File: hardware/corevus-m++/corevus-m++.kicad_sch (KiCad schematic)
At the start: 156 parts, among them J1 USB 2.0, J4 Power In, J4 XH, J5 Power In, J5 XH, J6 1x2P, SW3 BOOT, SW3 RST, T1 3.3V, T1 CS, T1 Diag, T1 Dir, T1 En, T1 Gnd, T1 MISO, T1 MOSI, T1 SClk, T1 Step, T1 Therm, T1 V_{SA}, U1 AMS1117-3.3, U2 TPS61040DBV, U3 STM32H750VBTx, Y1 12 MHz

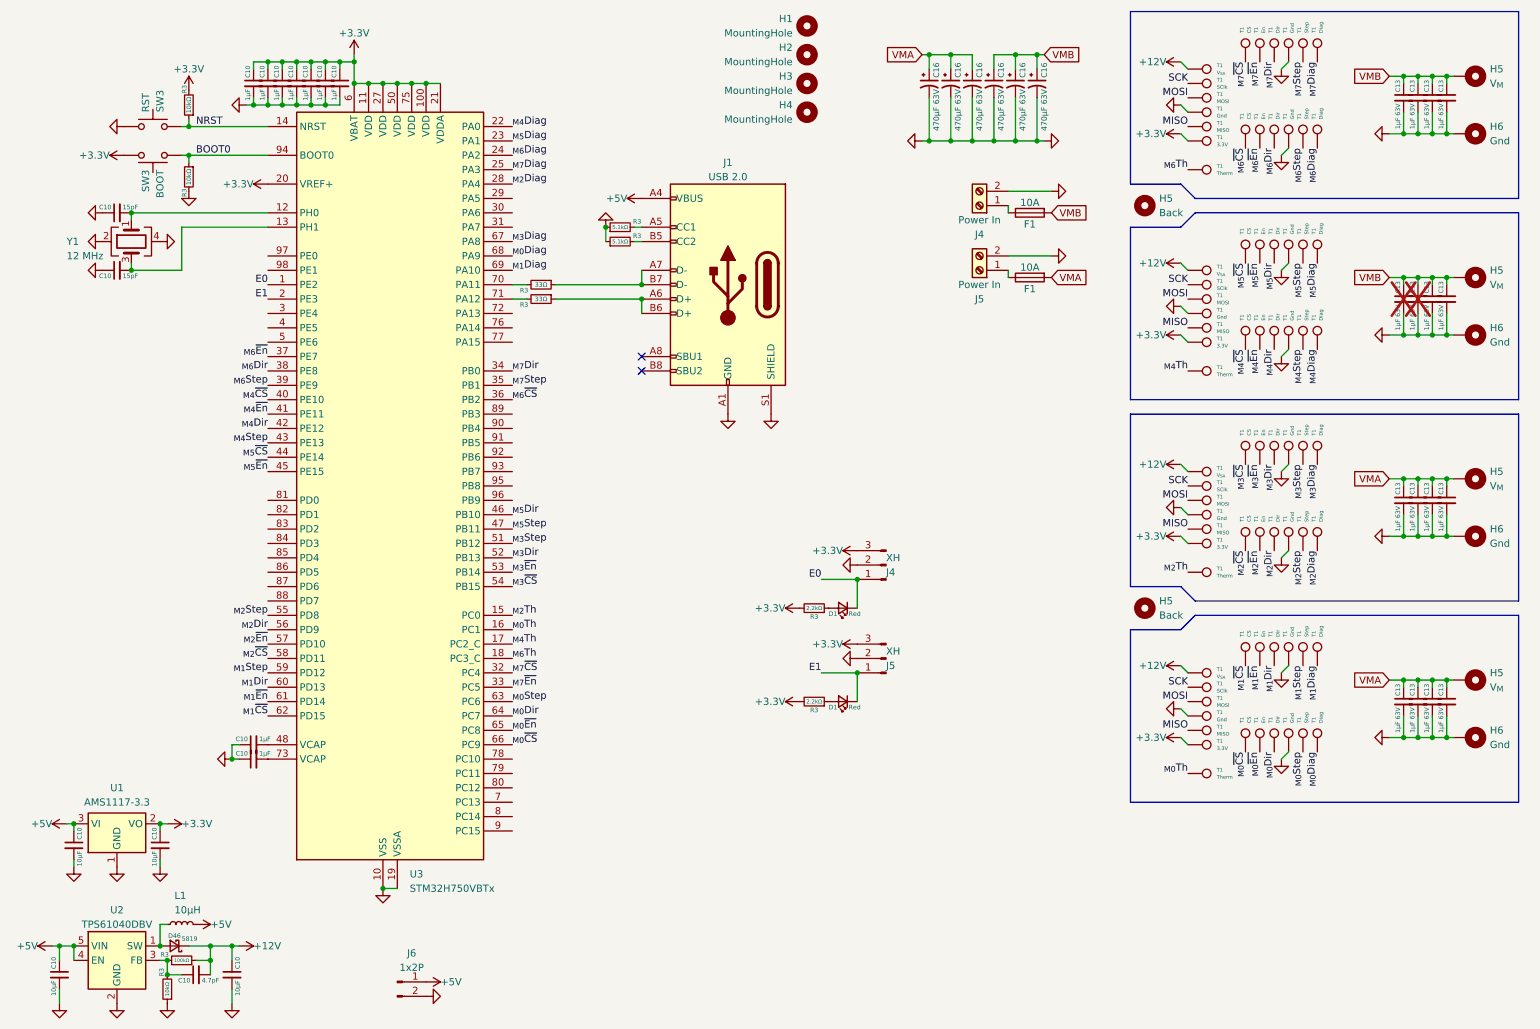
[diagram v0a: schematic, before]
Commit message: corevus toolboard v0.2 release (working), corevus-g v0.2 release (very much not working), m++ v0.1 (not working, needs a lot of bodges)
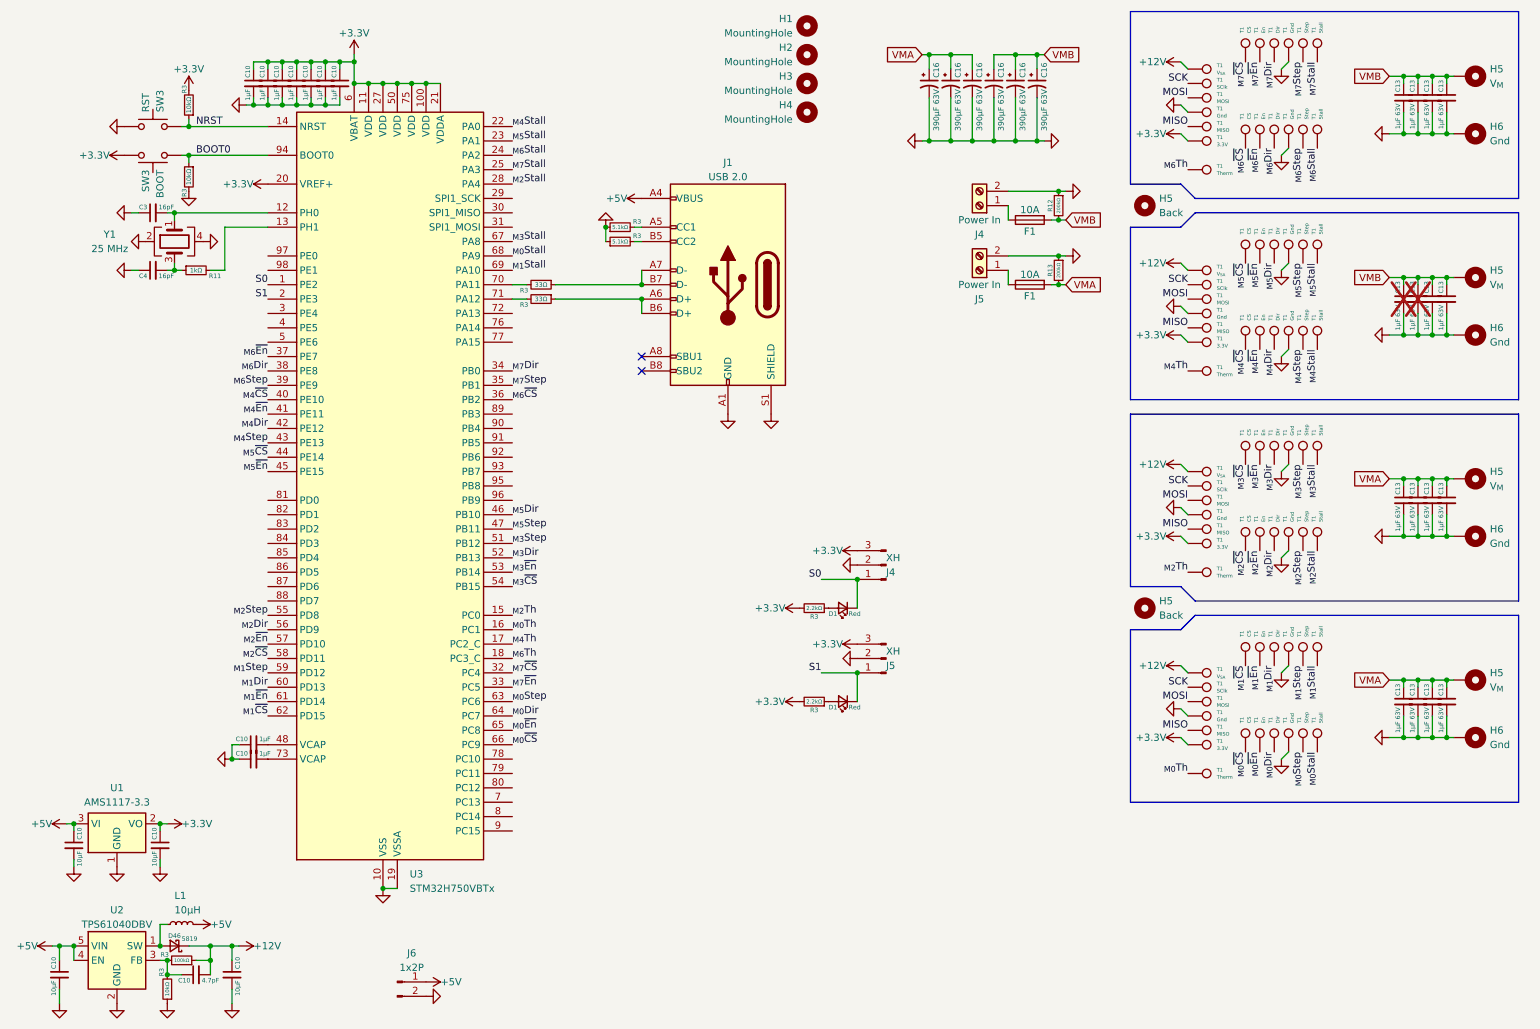
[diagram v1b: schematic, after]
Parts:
- removed C10 (x2): 15pF, AlphaLib:0402C, symbol Device:C_Small
- added C3, C4: 16pF, AlphaLib:0402C, symbol Device:C_Small
- added R11: 1kΩ, AlphaLib:0402R, symbol Device:R_Small
- added R12, R13: 200kΩ, AlphaLib:0402R, symbol Device:R_Small
- C16: value 470μF 63V -> 390μF 63V
- F1: footprint corevus:XF-505P -> corevus:XF-506P
- L1: footprint Inductor_SMD:L_0805_2012Metric -> corevus:L_Changjiang_FTC2520
- T1: value Diag -> Stall
- Y1: value 12 MHz -> 25 MHz
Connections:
- net GND: now also C3.1, C4.1, R12.1, R13.1
- net VMA: now also R13.2
- net VMB: now also R12.2
- net at U3.12 (PH0), Y1.1: now also C3.2
- net at Y1.3: now also C4.2, R11.1; no longer U3.13 (PH1)
- net E0 renamed S0
- net E1 renamed S1
- net _{M0}Diag renamed _{M0}Stall
- net _{M1}Diag renamed _{M1}Stall
- net _{M2}Diag renamed _{M2}Stall
- net _{M3}Diag renamed _{M3}Stall
- net _{M4}Diag renamed _{M4}Stall
- net _{M5}Diag renamed _{M5}Stall
- net _{M6}Diag renamed _{M6}Stall
- net _{M7}Diag renamed _{M7}Stall
- new net: R11.2, U3.13 (PH1)
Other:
- moved on the sheet: F1
